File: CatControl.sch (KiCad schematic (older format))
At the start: 6 parts, among them J2 CAT, U2 FT232RL

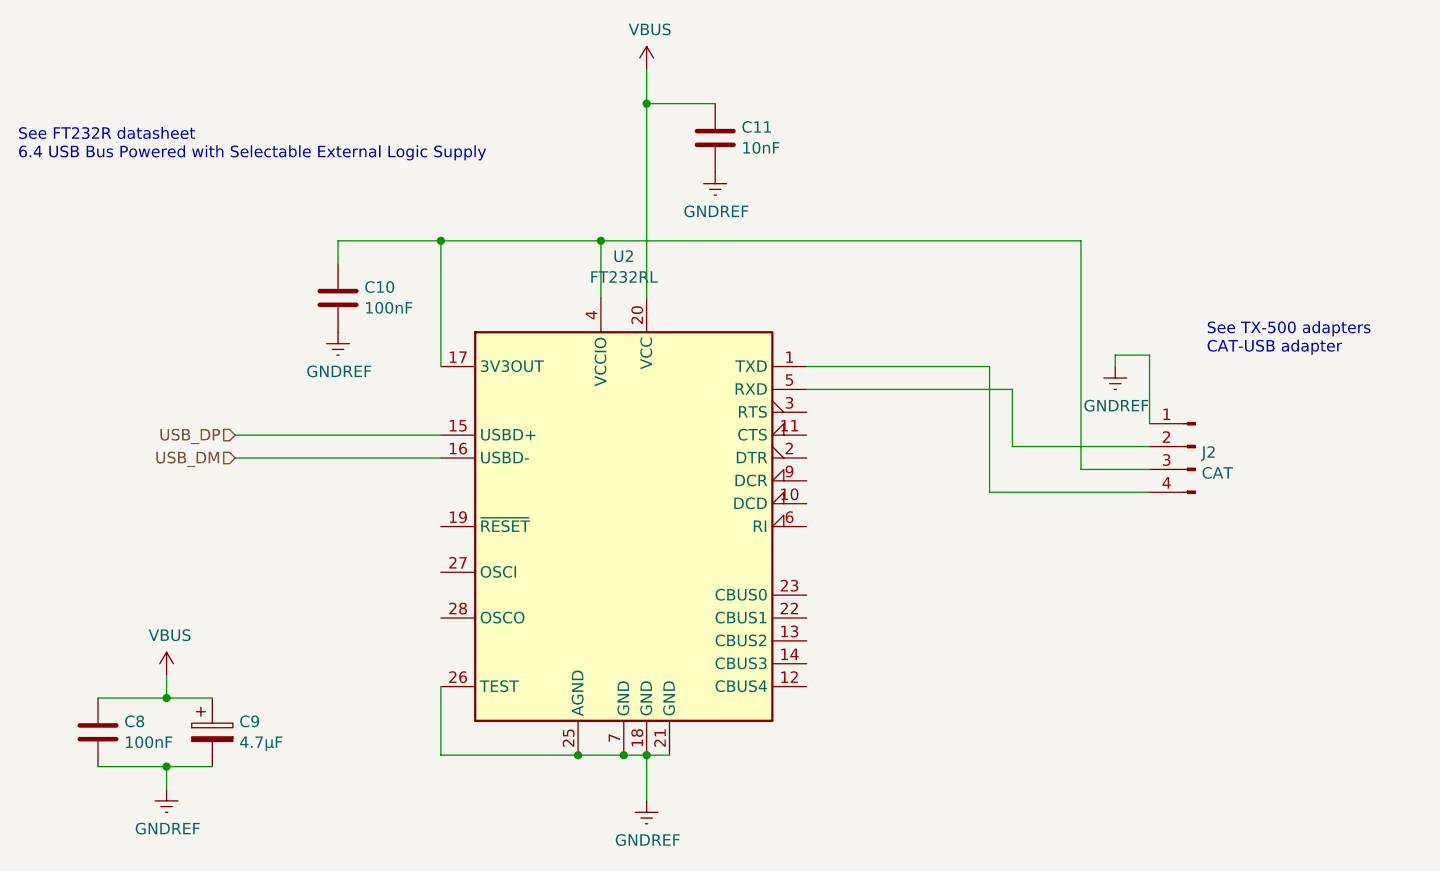
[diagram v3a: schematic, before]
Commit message: Swap TUSB4041I for TUSB2036
The 4041 does more than I need it to, so use the 2036 instead.
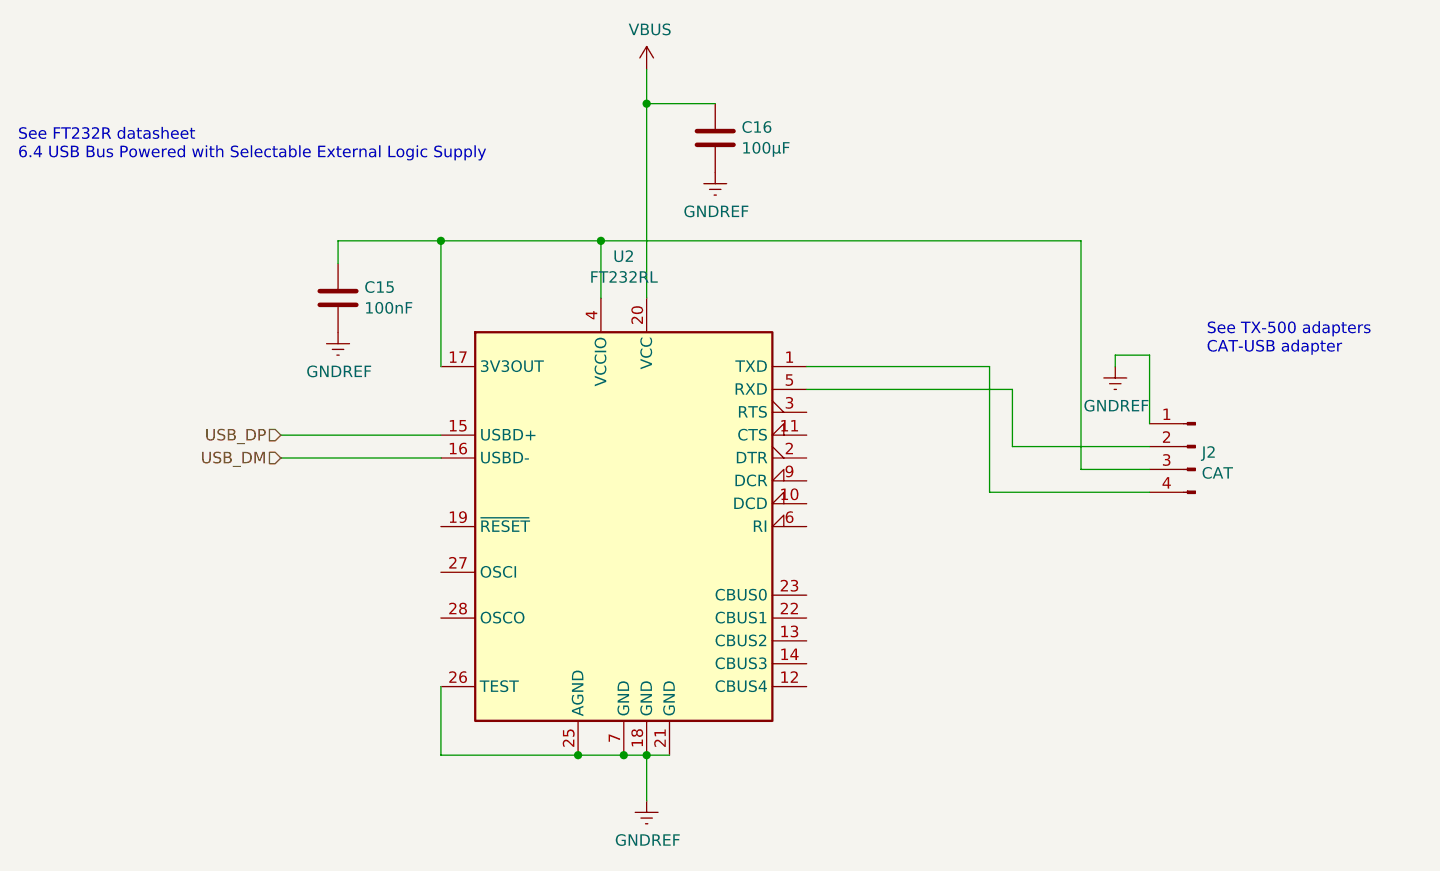
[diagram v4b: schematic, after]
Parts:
- removed C8: 100nF, Capacitor_SMD:C_1210_3225Metric, symbol Device:C
- removed C9: 4.7μF, Capacitor_SMD:CP_Elec_4x3, symbol Device:CP
- C16: renamed from C11; value 10nF -> 100μF; footprint Capacitor_SMD:C_1210_3225Metric -> Capacitor_SMD:CP_Elec_4x3
- renumbered C10 to C15
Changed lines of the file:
@@
 $Descr A4 11693 8268
 encoding utf-8
-Sheet 6 6
+Sheet 5 6
 Title ""
 Date ""
@@
 	-1   0    0    -1
 $EndComp
-Text HLabel 3750 3200 0    50   Input ~ 0
-USB_DP
-Text HLabel 3750 3300 0    50   Input ~ 0
-USB_DM
-Wire Wire Line
-	3750 3300 4650 3300
-Wire Wire Line
-	4650 3200 3750 3200
 $Comp
 L power:GNDREF #PWR0118
@@
 Wire Wire Line
 	5350 2350 7450 2350
-$Comp
-L power:VBUS #PWR0121
-U 1 1 605C93BD
-P 3450 4250
-F 0 "#PWR0121" H 3450 4100 50  0001 C CNN
-F 1 "VBUS" H 3465 4423 50  0000 C CNN
-F 2 "" H 3450 4250 50  0001 C CNN
-F 3 "" H 3450 4250 50  0001 C CNN
-	1    3450 4250
-	1    0    0    -1
-$EndComp
-$Comp
-L power:GNDREF #PWR0122
-U 1 1 605C99BA
-P 3450 4750
-F 0 "#PWR0122" H 3450 4500 50  0001 C CNN
-F 1 "GNDREF" H 3455 4577 50  0000 C CNN
-F 2 "" H 3450 4750 50  0001 C CNN
-F 3 "" H 3450 4750 50  0001 C CNN
-	1    3450 4750
-	1    0    0    -1
-$EndComp
-$Comp
-L Device:C C8
-U 1 1 605CA219
-P 3150 4500
-F 0 "C8" H 3265 4546 50  0000 L CNN
-F 1 "100nF" H 3265 4455 50  0000 L CNN
-F 2 "Capacitor_SMD:C_1210_3225Metric" H 3188 4350 50  0001 C CNN
-F 3 "~" H 3150 4500 50  0001 C CNN
-	1    3150 4500
-	1    0    0    -1
-$EndComp
-$Comp
-L Device:CP C9
-U 1 1 605CB7E6
-P 3650 4500
-F 0 "C9" H 3768 4546 50  0000 L CNN
-F 1 "4.7μF" H 3768 4455 50  0000 L CNN
-F 2 "Capacitor_SMD:CP_Elec_4x3" H 3688 4350 50  0001 C CNN
-F 3 "~" H 3650 4500 50  0001 C CNN
-	1    3650 4500
-	1    0    0    -1
-$EndComp
-Wire Wire Line
-	3150 4350 3450 4350
-Wire Wire Line
-	3450 4250 3450 4350
-Connection ~ 3450 4350
-Wire Wire Line
-	3450 4350 3650 4350
-Wire Wire Line
-	3150 4650 3450 4650
-Wire Wire Line
-	3450 4650 3450 4750
-Connection ~ 3450 4650
-Wire Wire Line
-	3450 4650 3650 4650
 Text Notes 2800 2000 0    50   ~ 0
 See FT232R datasheet\n6.4 USB Bus Powered with Selectable External Logic Supply
@@
 See TX-500 adapters\nCAT-USB adapter
 $Comp
-L Device:C C11
+L Device:C C16
 U 1 1 604C7383
 P 5850 1900
-F 0 "C11" H 5965 1946 50  0000 L CNN
-F 1 "10nF" H 5965 1855 50  0000 L CNN
-F 2 "Capacitor_SMD:C_1210_3225Metric" H 5888 1750 50  0001 C CNN
+F 0 "C16" H 5965 1946 50  0000 L CNN
+F 1 "100μF" H 5965 1855 50  0000 L CNN
+F 2 "Capacitor_SMD:CP_Elec_4x3" H 5888 1750 50  0001 C CNN
 F 3 "~" H 5850 1900 50  0001 C CNN
 	1    5850 1900
@@
 	5550 1750 5550 2600
 $Comp
-L Device:C C10
+L Device:C C15
 U 1 1 604CE119
 P 4200 2600
-F 0 "C10" H 4315 2646 50  0000 L CNN
+F 0 "C15" H 4315 2646 50  0000 L CNN
 F 1 "100nF" H 4315 2555 50  0000 L CNN
 F 2 "Capacitor_SMD:C_1210_3225Metric" H 4238 2450 50  0001 C CNN
@@
 	4200 2350 4200 2450
 Connection ~ 4650 2350
+Text HLabel 3950 3200 0    50   Input ~ 0
+USB_DP
+Text HLabel 3950 3300 0    50   Input ~ 0
+USB_DM
+Wire Wire Line
+	3950 3200 4650 3200
+Wire Wire Line
+	3950 3300 4650 3300
 $EndSCHEMATC

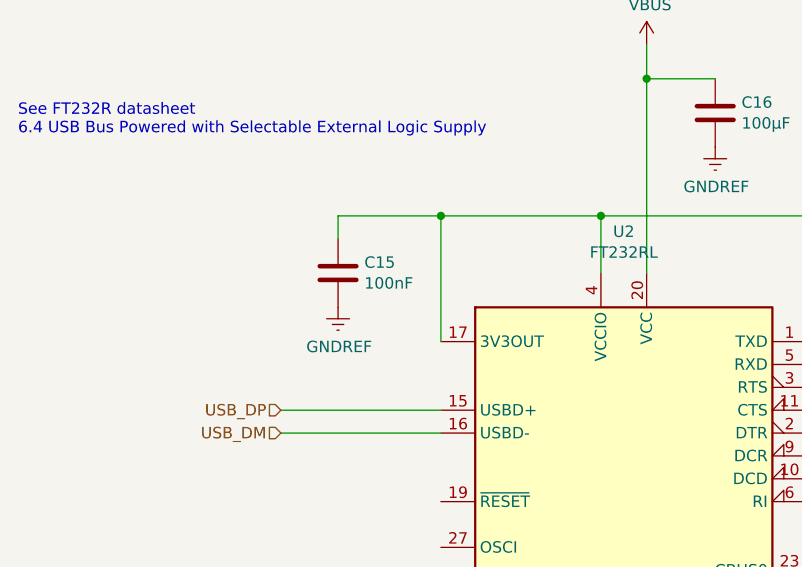
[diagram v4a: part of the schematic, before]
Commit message: Add BOM and clarify some footprints
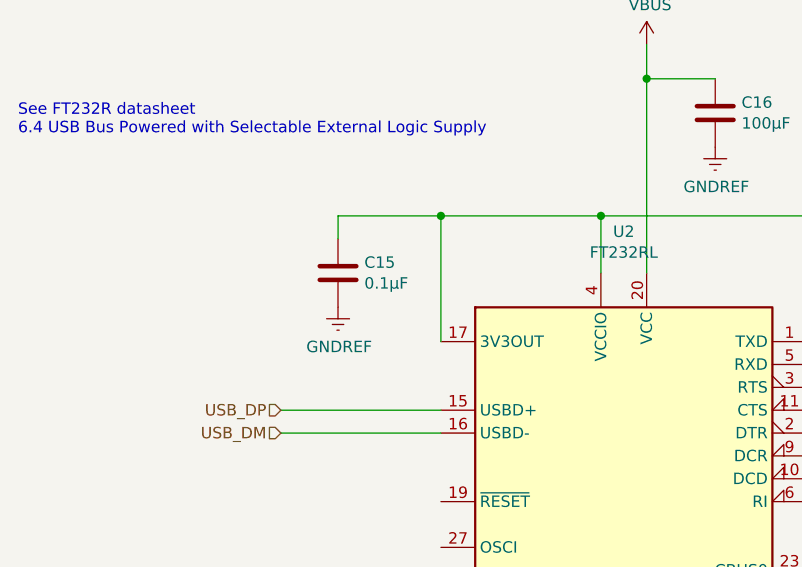
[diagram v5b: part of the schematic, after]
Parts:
- C15: value 100nF -> 0.1μF; Manufacturer_Name (none) -> KEMET; Manufacturer_Part_Number (none) -> C1210C104K5HACAUTO; Price (none) -> 0.5; Vendor (none) -> Mouser; Vendor Part Number (none) -> 80-C1210C104K5HAUTO
- C16: footprint Capacitor_SMD:CP_Elec_4x3 -> Capacitor_SMD:C_1210_3225Metric; Manufacturer_Name (none) -> AVX; Manufacturer_Part_Number (none) -> TPST107M004R0500; Price (none) -> 0.93; Vendor (none) -> Mouser; Vendor Part Number (none) -> 581-TPST107M004R0500
- J2: Description (none) -> TX-500 CAT Interconnect; Manufacturer_Name (none) -> JST; Manufacturer_Part_Number (none) -> B4B-PH-SM4-TB; Price (none) -> 0.35; Vendor (none) -> Mouser; Vendor Part Number (none) -> 485-4392
- U2: Description (none) -> UART; Manufacturer_Name (none) -> FTDI; Manufacturer_Part_Number (none) -> FT232RL; Price (none) -> 4.6; Vendor (none) -> Mouser; Vendor Part Number (none) -> 895-FT232RL-TUBE
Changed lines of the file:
@@
 F 2 "Package_SO:SSOP-28_5.3x10.2mm_P0.65mm" H 6550 2700 50  0001 C CNN
 F 3 "https://www.ftdichip.com/Support/Documents/DataSheets/ICs/DS_FT232R.pdf" H 5450 3600 50  0001 C CNN
+F 4 "UART" H 5450 4881 50  0001 C CNN "Description"
+F 5 "FTDI" H 5450 4881 50  0001 C CNN "Manufacturer_Name"
+F 6 "FT232RL" H 5450 4881 50  0001 C CNN "Manufacturer_Part_Number"
+F 7 "4.6" H 5450 4881 50  0001 C CNN "Price"
+F 8 "895-FT232RL-TUBE" H 5450 4881 50  0001 C CNN "Vendor Part Number"
+F 9 "Mouser" H 5450 4881 50  0001 C CNN "Vendor"
 	1    5450 3600
 	1    0    0    -1
@@
 F 1 "CAT" H 7922 3133 50  0000 R CNN
 F 2 "Connector_JST:JST_PH_B4B-PH-SM4-TB_1x04-1MP_P2.00mm_Vertical" H 7950 3250 50  0001 C CNN
-F 3 "~" H 7950 3250 50  0001 C CNN
+F 3 "https://www.mouser.com/datasheet/2/737/4389_C13924-001_CCP-W20-03-BK-SMT-R-A-1708610.pdf" H 7950 3250 50  0001 C CNN
+F 4 "TX-500 CAT Interconnect" H 7922 3324 50  0001 C CNN "Description"
+F 5 "JST" H 7922 3324 50  0001 C CNN "Manufacturer_Name"
+F 6 "B4B-PH-SM4-TB" H 7922 3324 50  0001 C CNN "Manufacturer_Part_Number"
+F 7 "0.35" H 7922 3324 50  0001 C CNN "Price"
+F 8 "485-4392" H 7922 3324 50  0001 C CNN "Vendor Part Number"
+F 9 "Mouser" H 7922 3324 50  0001 C CNN "Vendor"
 	1    7950 3250
 	-1   0    0    -1
@@
 	1    0    0    -1
 $EndComp
+$Comp
+L power:GNDREF #PWR0119
+U 1 1 605C410A
+P 7600 2900
+F 0 "#PWR0119" H 7600 2650 50  0001 C CNN
+F 1 "GNDREF" H 7605 2727 50  0000 C CNN
+F 2 "" H 7600 2900 50  0001 C CNN
+F 3 "" H 7600 2900 50  0001 C CNN
+	1    7600 2900
+	1    0    0    -1
+$EndComp
+$Comp
+L power:VBUS #PWR0120
+U 1 1 605C5EC8
+P 5550 1600
+F 0 "#PWR0120" H 5550 1450 50  0001 C CNN
+F 1 "VBUS" H 5565 1773 50  0000 C CNN
+F 2 "" H 5550 1600 50  0001 C CNN
+F 3 "" H 5550 1600 50  0001 C CNN
+	1    5550 1600
+	1    0    0    -1
+$EndComp
+$Comp
+L Device:C C16
+U 1 1 604C7383
+P 5850 1900
+F 0 "C16" H 5965 1946 50  0000 L CNN
+F 1 "100μF" H 5965 1855 50  0000 L CNN
+F 2 "Capacitor_SMD:C_1210_3225Metric" H 5888 1750 50  0001 C CNN
+F 3 "https://www.mouser.com/datasheet/2/40/TPS-2066671.pdf" H 5850 1900 50  0001 C CNN
+F 4 "AVX" H 5965 2046 50  0001 C CNN "Manufacturer_Name"
+F 5 "TPST107M004R0500" H 5965 2046 50  0001 C CNN "Manufacturer_Part_Number"
+F 6 "0.93" H 5965 2046 50  0001 C CNN "Price"
+F 7 "581-TPST107M004R0500" H 5965 2046 50  0001 C CNN "Vendor Part Number"
+F 8 "Mouser" H 5965 2046 50  0001 C CNN "Vendor"
+	1    5850 1900
+	1    0    0    -1
+$EndComp
+$Comp
+L power:GNDREF #PWR0123
+U 1 1 604C84F9
+P 5850 2050
+F 0 "#PWR0123" H 5850 1800 50  0001 C CNN
+F 1 "GNDREF" H 5855 1877 50  0000 C CNN
+F 2 "" H 5850 2050 50  0001 C CNN
+F 3 "" H 5850 2050 50  0001 C CNN
+	1    5850 2050
+	1    0    0    -1
+$EndComp
+$Comp
+L Device:C C15
+U 1 1 604CE119
+P 4200 2600
+F 0 "C15" H 4315 2646 50  0000 L CNN
+F 1 "0.1μF" H 4315 2555 50  0000 L CNN
+F 2 "Capacitor_SMD:C_1210_3225Metric" H 4238 2450 50  0001 C CNN
+F 3 "https://www.mouser.com/datasheet/2/212/KEM_C1007_X8R_ULTRA_150C_SMD-1102703.pdf" H 4200 2600 50  0001 C CNN
+F 4 "KEMET" H 4315 2746 50  0001 C CNN "Manufacturer_Name"
+F 5 "C1210C104K5HACAUTO" H 4315 2746 50  0001 C CNN "Manufacturer_Part_Number"
+F 6 "0.5" H 4315 2746 50  0001 C CNN "Price"
+F 7 "80-C1210C104K5HAUTO" H 4315 2746 50  0001 C CNN "Vendor Part Number"
+F 8 "Mouser" H 4315 2746 50  0001 C CNN "Vendor"
+	1    4200 2600
+	1    0    0    -1
+$EndComp
+$Comp
+L power:GNDREF #PWR0124
+U 1 1 604CEB86
+P 4200 2750
+F 0 "#PWR0124" H 4200 2500 50  0001 C CNN
+F 1 "GNDREF" H 4205 2577 50  0000 C CNN
+F 2 "" H 4200 2750 50  0001 C CNN
+F 3 "" H 4200 2750 50  0001 C CNN
+	1    4200 2750
+	1    0    0    -1
+$EndComp
+Text Notes 2800 2000 0    50   ~ 0
+See FT232R datasheet\n6.4 USB Bus Powered with Selectable External Logic Supply
+Text Notes 8000 2850 0    50   ~ 0
+See TX-500 adapters\nCAT-USB adapter
+Text HLabel 3950 3200 0    50   Input ~ 0
+USB_DP
+Text HLabel 3950 3300 0    50   Input ~ 0
+USB_DM
 Wire Wire Line
 	5450 4600 5550 4600
 Wire Wire Line
 	5550 4600 5650 4600
-Connection ~ 5550 4600
 Wire Wire Line
 	5550 4600 5550 4800
@@
 Wire Wire Line
 	7600 2850 7600 2900
-$Comp
-L power:GNDREF #PWR0119
-U 1 1 605C410A
-P 7600 2900
-F 0 "#PWR0119" H 7600 2650 50  0001 C CNN
-F 1 "GNDREF" H 7605 2727 50  0000 C CNN
-F 2 "" H 7600 2900 50  0001 C CNN
-F 3 "" H 7600 2900 50  0001 C CNN
-	1    7600 2900
-	1    0    0    -1
-$EndComp
 Wire Wire Line
 	4650 4300 4650 4600
@@
 Wire Wire Line
 	5250 4600 5450 4600
-Connection ~ 5250 4600
-Connection ~ 5450 4600
-$Comp
-L power:VBUS #PWR0120
-U 1 1 605C5EC8
-P 5550 1600
-F 0 "#PWR0120" H 5550 1450 50  0001 C CNN
-F 1 "VBUS" H 5565 1773 50  0000 C CNN
-F 2 "" H 5550 1600 50  0001 C CNN
-F 3 "" H 5550 1600 50  0001 C CNN
-	1    5550 1600
-	1    0    0    -1
-$EndComp
 Wire Wire Line
 	5350 2350 5350 2600
-Connection ~ 5350 2350
 Wire Wire Line
 	5350 2350 7450 2350
-Text Notes 2800 2000 0    50   ~ 0
-See FT232R datasheet\n6.4 USB Bus Powered with Selectable External Logic Supply
-Text Notes 8000 2850 0    50   ~ 0
-See TX-500 adapters\nCAT-USB adapter
-$Comp
-L Device:C C16
-U 1 1 604C7383
-P 5850 1900
-F 0 "C16" H 5965 1946 50  0000 L CNN
-F 1 "100μF" H 5965 1855 50  0000 L CNN
-F 2 "Capacitor_SMD:CP_Elec_4x3" H 5888 1750 50  0001 C CNN
-F 3 "~" H 5850 1900 50  0001 C CNN
-	1    5850 1900
-	1    0    0    -1
-$EndComp
-$Comp
-L power:GNDREF #PWR0123
-U 1 1 604C84F9
-P 5850 2050
-F 0 "#PWR0123" H 5850 1800 50  0001 C CNN
-F 1 "GNDREF" H 5855 1877 50  0000 C CNN
-F 2 "" H 5850 2050 50  0001 C CNN
-F 3 "" H 5850 2050 50  0001 C CNN
-	1    5850 2050
-	1    0    0    -1
-$EndComp
 Wire Wire Line
 	5550 1600 5550 1750
 Wire Wire Line
 	5850 1750 5550 1750
-Connection ~ 5550 1750
 Wire Wire Line
 	5550 1750 5550 2600
-$Comp
-L Device:C C15
-U 1 1 604CE119
-P 4200 2600
-F 0 "C15" H 4315 2646 50  0000 L CNN
-F 1 "100nF" H 4315 2555 50  0000 L CNN
-F 2 "Capacitor_SMD:C_1210_3225Metric" H 4238 2450 50  0001 C CNN
-F 3 "~" H 4200 2600 50  0001 C CNN
-	1    4200 2600
-	1    0    0    -1
-$EndComp
-$Comp
-L power:GNDREF #PWR0124
-U 1 1 604CEB86
-P 4200 2750
-F 0 "#PWR0124" H 4200 2500 50  0001 C CNN
-F 1 "GNDREF" H 4205 2577 50  0000 C CNN
-F 2 "" H 4200 2750 50  0001 C CNN
-F 3 "" H 4200 2750 50  0001 C CNN
-	1    4200 2750
-	1    0    0    -1
-$EndComp
 Wire Wire Line
 	4650 2350 4200 2350
 Wire Wire Line
 	4200 2350 4200 2450
-Connection ~ 4650 2350
-Text HLabel 3950 3200 0    50   Input ~ 0
-USB_DP
-Text HLabel 3950 3300 0    50   Input ~ 0
-USB_DM
 Wire Wire Line
 	3950 3200 4650 3200
 Wire Wire Line
 	3950 3300 4650 3300
+Connection ~ 5550 4600
+Connection ~ 5250 4600
+Connection ~ 5450 4600
+Connection ~ 5350 2350
+Connection ~ 5550 1750
+Connection ~ 4650 2350
 $EndSCHEMATC
